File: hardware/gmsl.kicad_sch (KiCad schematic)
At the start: 1 part, among them U1 MAX96717GTJ/VY+

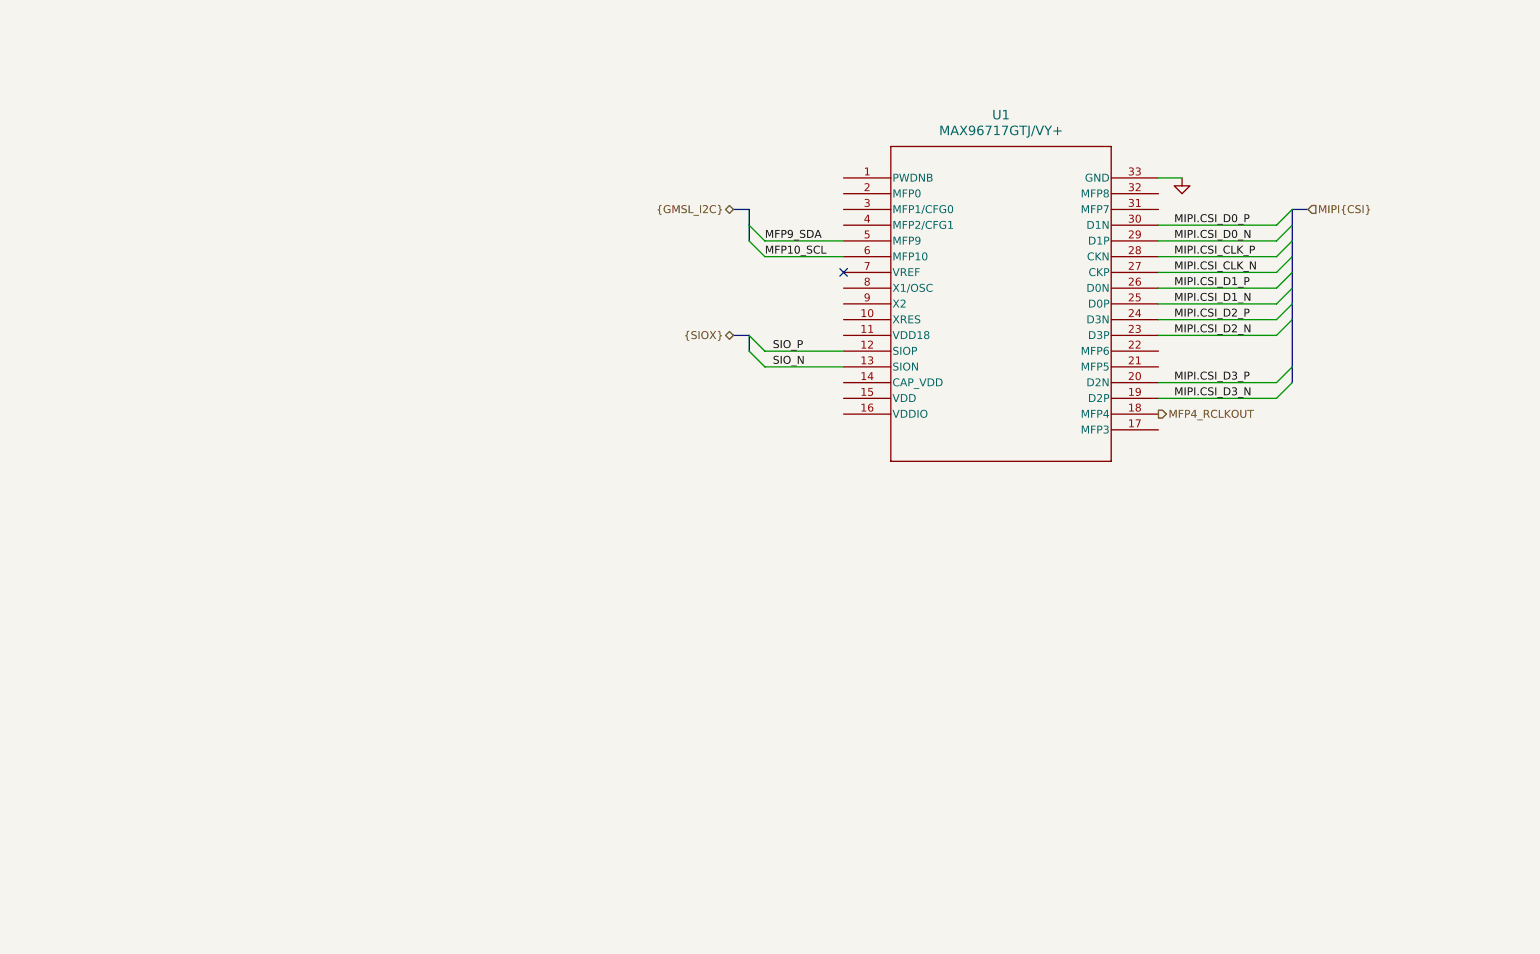
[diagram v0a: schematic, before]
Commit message: finished rough pass on max96717, need cfgs. added notes to imx219 inck tolerance.
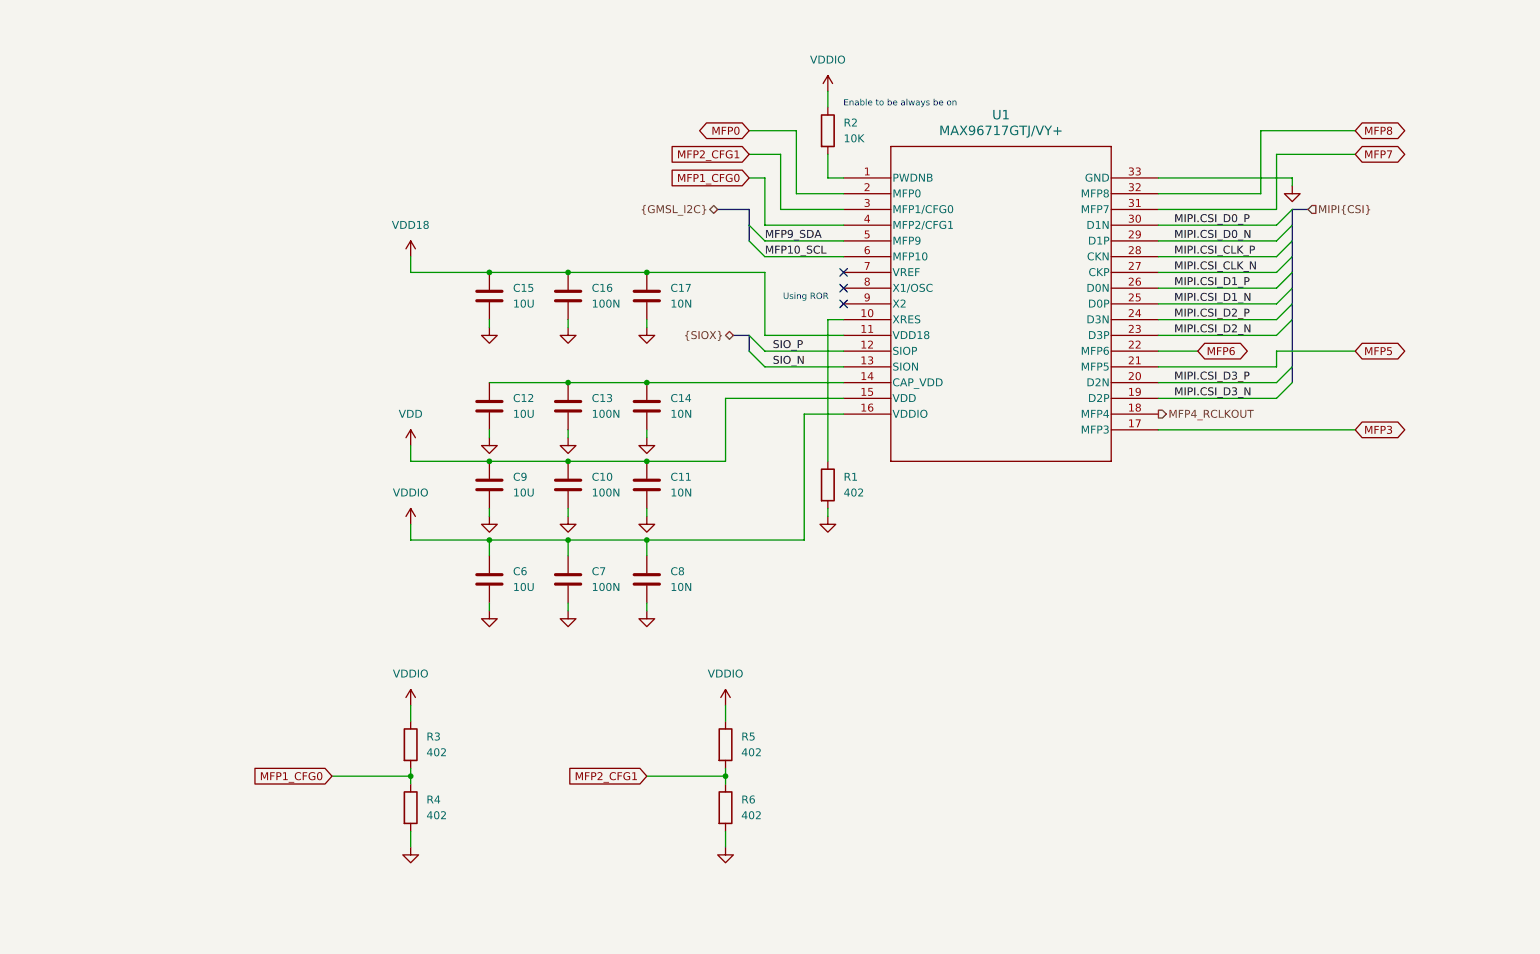
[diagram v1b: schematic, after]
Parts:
- added C10, C13, C16, C7: 100N, Capacitor_SMD:C_0402_1005Metric, symbol Device:C
- added C11, C14, C17, C8: 10N, Capacitor_SMD:C_0402_1005Metric, symbol Device:C
- added C12, C15, C6, C9: 10U, Capacitor_SMD:C_0402_1005Metric, symbol Device:C
- added R1, R3, R4, R5, R6: 402, Resistor_SMD:R_0402_1005Metric, symbol Device:R
- added R2: 10K, Resistor_SMD:R_0402_1005Metric, symbol Device:R
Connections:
- net GND: now also C10.2, C11.2, C12.2, C13.2, C14.2, C15.2, C16.2, C17.2, C6.2, C7.2, C8.2, C9.2, R1.2, R4.2, R6.2
- net at U1.1 (PWDNB): now also R2.2
- net at U1.10 (XRES): now also R1.1
- net VDD18: now reaches U1.11 (VDD18)
- net VDD18: now also C15.1, C16.1, C17.1
- net at U1.14 (CAP_VDD): now also C12.1, C13.1, C14.1
- net VDD: now reaches U1.15 (VDD)
- net VDD: now also C10.1, C11.1, C9.1
- net VDDIO: now reaches U1.16 (VDDIO)
- net VDDIO: now also C6.1, C7.1, C8.1, R2.1, R3.1, R5.1
- net MFP3: now reaches U1.17 (MFP3)
- net MFP0: now reaches U1.2 (MFP0)
- net MFP5: now reaches U1.21 (MFP5)
- net MFP6: now reaches U1.22 (MFP6)
- net MFP2_CFG1: now reaches U1.3 (MFP1/CFG0)
- net MFP2_CFG1: now also R5.2, R6.1
- net MFP7: now reaches U1.31 (MFP7)
- net MFP8: now reaches U1.32 (MFP8)
- net MFP1_CFG0: now reaches U1.4 (MFP2/CFG1)
- net MFP1_CFG0: now also R3.2, R4.1
- no-connect marks 1 -> 3
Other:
- note added: "Enable to be always be on"
- note added: "Using ROR"

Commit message: cleaned up serializer with comments and project hierarchy
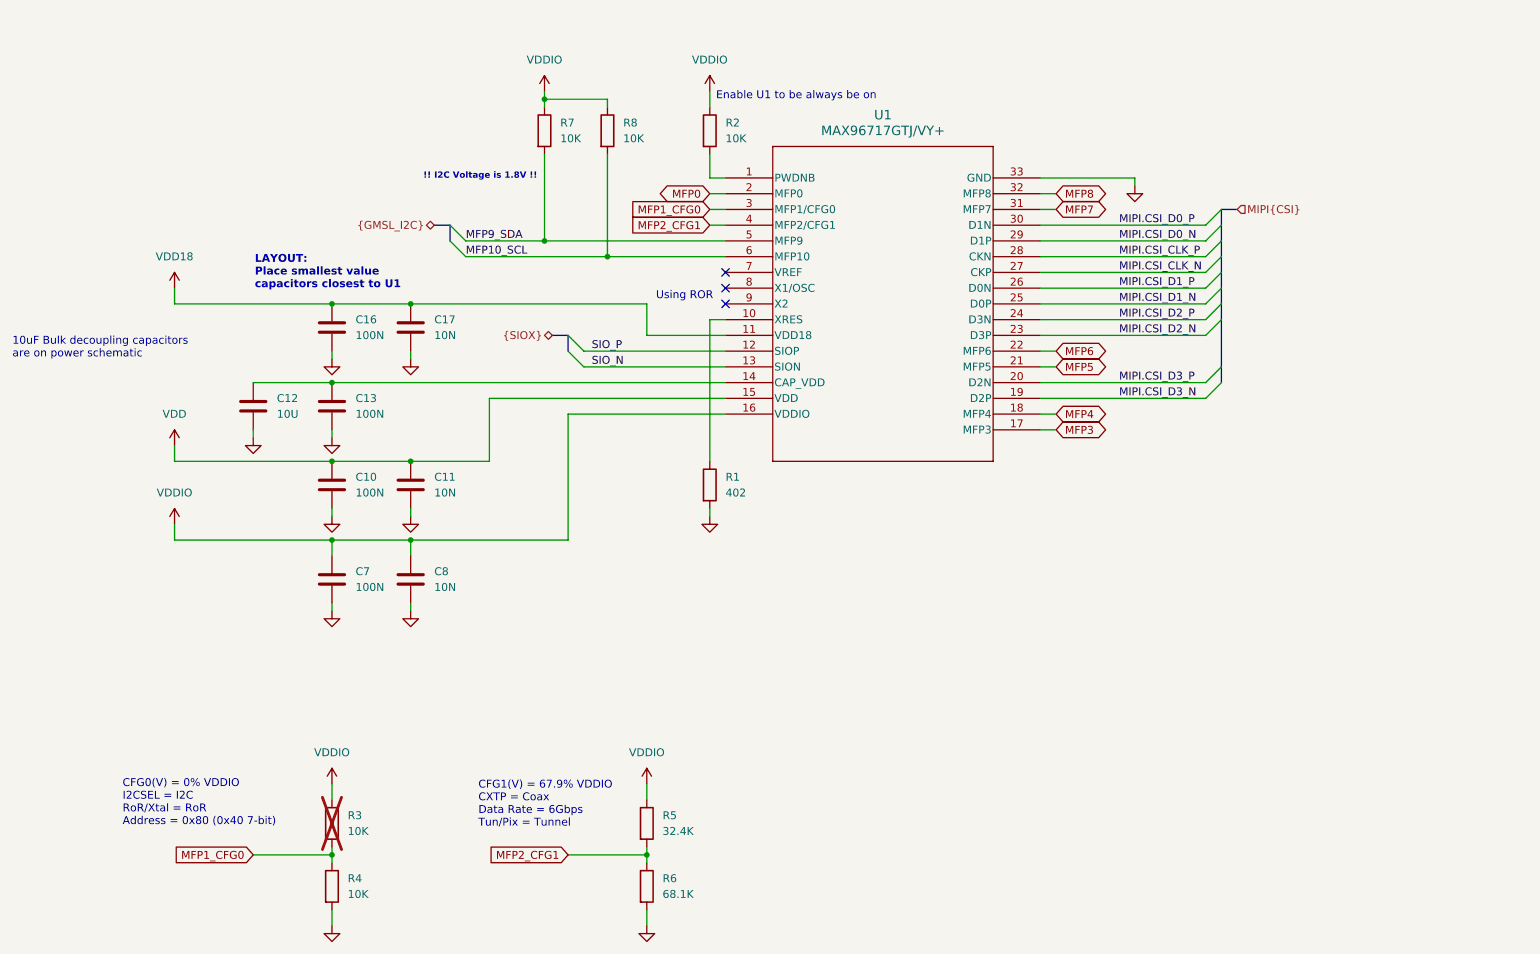
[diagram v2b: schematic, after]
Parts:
- removed C14: 10N, Capacitor_SMD:C_0402_1005Metric, symbol Device:C
- removed C15, C6, C9: 10U, Capacitor_SMD:C_0402_1005Metric, symbol Device:C
- added R7, R8: 10K, Resistor_SMD:R_0402_1005Metric, symbol Device:R
- R3: value 402 -> 10K; now not fitted
- R4: value 402 -> 10K
- R5: value 402 -> 32.4K
- R6: value 402 -> 68.1K
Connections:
- net MFP10_SCL: now also R8.2
- net MFP1_CFG0: now also U1.3 (MFP1/CFG0); no longer U1.4 (MFP2/CFG1)
- net MFP2_CFG1: now also U1.4 (MFP2/CFG1); no longer U1.3 (MFP1/CFG0)
- net MFP9_SDA: now also R7.2
- net VDDIO: now also R7.1, R8.1
- net MFP4_RCLKOUT renamed MFP4
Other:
- note added: "!! I2C Voltage is 1.8V !!"
- note added: "10uF Bulk decoupling capacitors are on power schematic"
- note added: "CFG0(V) = 0% VDDIO I2CSEL = I2C RoR/Xtal = RoR Address = 0x80 (0x40 7-bit)"
- note added: "CFG1(V) = 67.9% VDDIO CXTP = Coax Data Rate = 6Gbps Tun/Pix = Tunnel"
- note added: "Enable U1 to be always be on"
- note added: "LAYOUT: Place smallest value capacitors closest to U1"
- note removed: "Enable to be always be on"
- moved on the sheet: C10, C12, C13, C16, C17, C7, C8, R1, R2, R4, R5, R6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

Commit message: cleaned up schematics
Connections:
- net MIPI.CSI_CLK_N: now also U1.28 (CKN); no longer U1.27 (CKP)
- net MIPI.CSI_CLK_P: now also U1.27 (CKP); no longer U1.28 (CKN)
- net MIPI.CSI_D0_N: now also U1.26 (D0N); no longer U1.29 (D1P)
- net MIPI.CSI_D0_P: now also U1.25 (D0P); no longer U1.30 (D1N)
- net MIPI.CSI_D1_N: now also U1.30 (D1N); no longer U1.25 (D0P)
- net MIPI.CSI_D1_P: now also U1.29 (D1P); no longer U1.26 (D0N)
- net MIPI.CSI_D2_N: now also U1.20 (D2N); no longer U1.23 (D3P)
- net MIPI.CSI_D2_P: now also U1.19 (D2P); no longer U1.24 (D3N)
- net MIPI.CSI_D3_N: now also U1.24 (D3N); no longer U1.19 (D2P)
- net MIPI.CSI_D3_P: now also U1.23 (D3P); no longer U1.20 (D2N)
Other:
- note removed: "!! I2C Voltage is 1.8V !!"
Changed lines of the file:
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@@
-		)
-	)
-	(text "!! I2C Voltage is 1.8V !!"
-		(exclude_from_sim no)
-		(at 90.932 55.626 0)
-		(effects
-			(font
-				(size 1.016 1.016)
-				(thickness 0.254)
-				(bold yes)
-				(color 255 0 0 1)
-			)
-			(justify left)
 		)
 	)
@@
 		)
 	)
-	(label "MIPI.CSI_D2_N"
+	(label "MIPI.CSI_D3_P"
 		(at 203.2 81.28 0)
 		(fields_autoplaced yes)
@@
 		)
 	)
-	(label "MIPI.CSI_D2_P"
+	(label "MIPI.CSI_D3_N"
 		(at 203.2 78.74 0)
 		(fields_autoplaced yes)
@@
 		)
 	)
-	(label "MIPI.CSI_CLK_P"
+	(label "MIPI.CSI_CLK_N"
 		(at 203.2 68.58 0)
 		(fields_autoplaced yes)
@@
 		)
 	)
-	(label "MIPI.CSI_D3_N"
+	(label "MIPI.CSI_D2_P"
 		(at 203.2 91.44 0)
 		(fields_autoplaced yes)
@@
 		)
 	)
-	(label "MIPI.CSI_CLK_N"
+	(label "MIPI.CSI_CLK_P"
 		(at 203.2 71.12 0)
 		(fields_autoplaced yes)
@@
 		)
 	)
-	(label "MIPI.CSI_D0_N"
+	(label "MIPI.CSI_D1_P"
 		(at 203.2 66.04 0)
 		(fields_autoplaced yes)
@@
 		)
 	)
-	(label "MIPI.CSI_D0_P"
+	(label "MIPI.CSI_D1_N"
 		(at 203.2 63.5 0)
 		(fields_autoplaced yes)
@@
 		)
 	)
-	(label "MIPI.CSI_D1_N"
+	(label "MIPI.CSI_D0_P"
 		(at 203.2 76.2 0)
 		(fields_autoplaced yes)
@@
 		)
 	)
-	(label "MIPI.CSI_D1_P"
+	(label "MIPI.CSI_D0_N"
 		(at 203.2 73.66 0)
 		(fields_autoplaced yes)
@@
 		)
 	)
-	(label "MIPI.CSI_D3_P"
+	(label "MIPI.CSI_D2_N"
 		(at 203.2 88.9 0)
 		(fields_autoplaced yes)

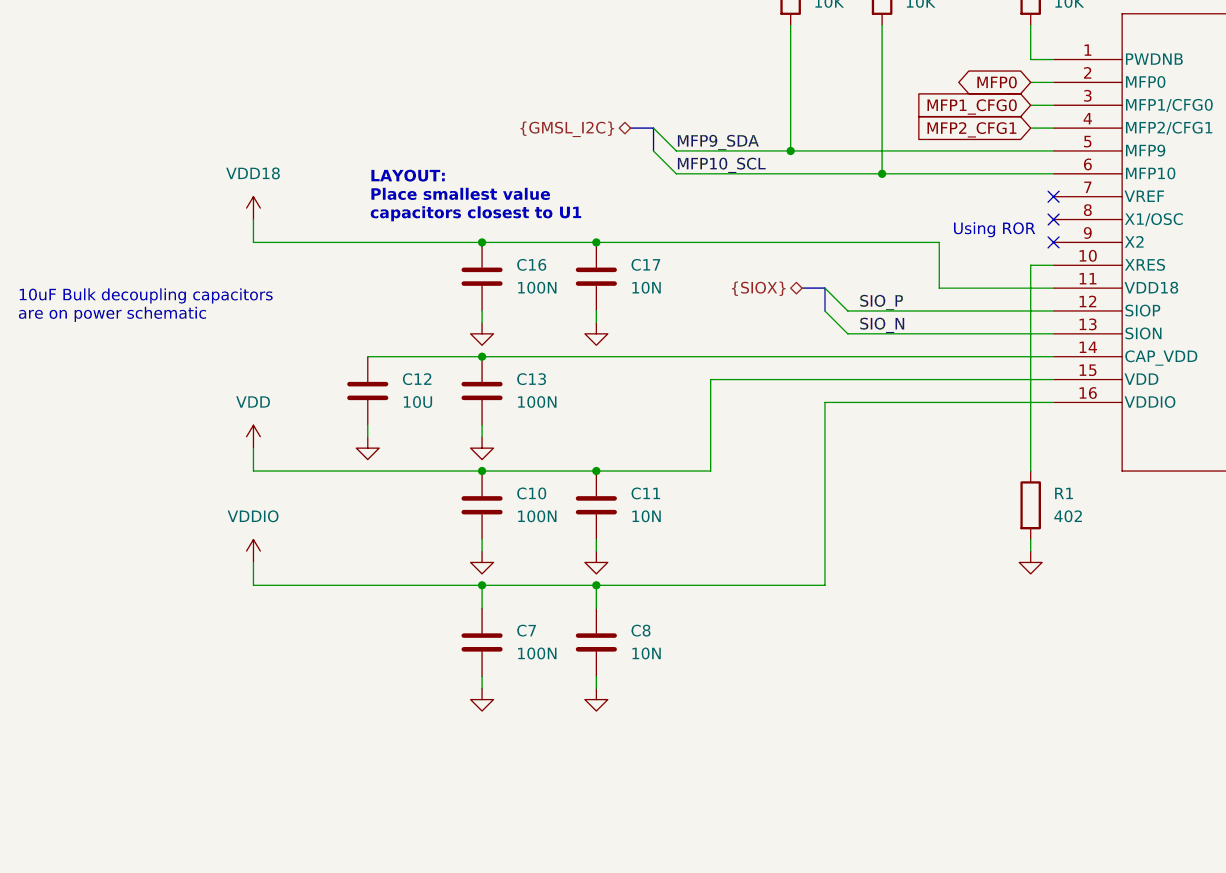
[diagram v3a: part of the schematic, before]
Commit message: started power, added smt fakra
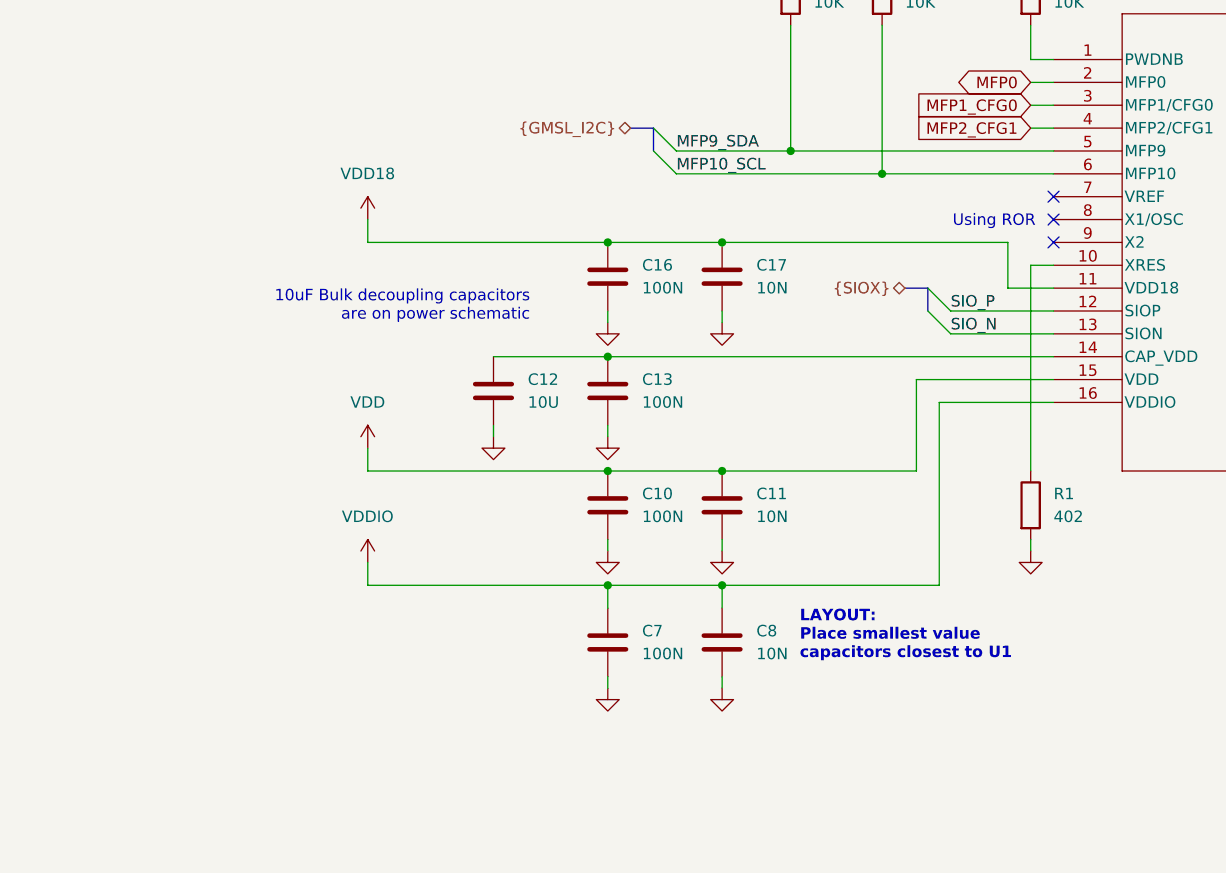
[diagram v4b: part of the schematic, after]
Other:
- moved on the sheet: C10, C11, C12, C13, C16, C17, C7, C8
